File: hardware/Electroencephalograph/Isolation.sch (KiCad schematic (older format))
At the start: 5 parts, among them U6 ADUM2401BRWZ

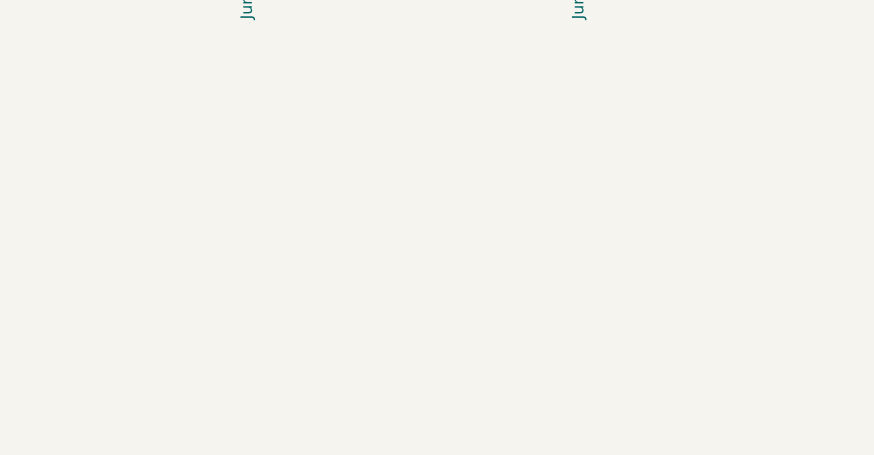
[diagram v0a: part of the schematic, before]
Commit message: power circuit supply added
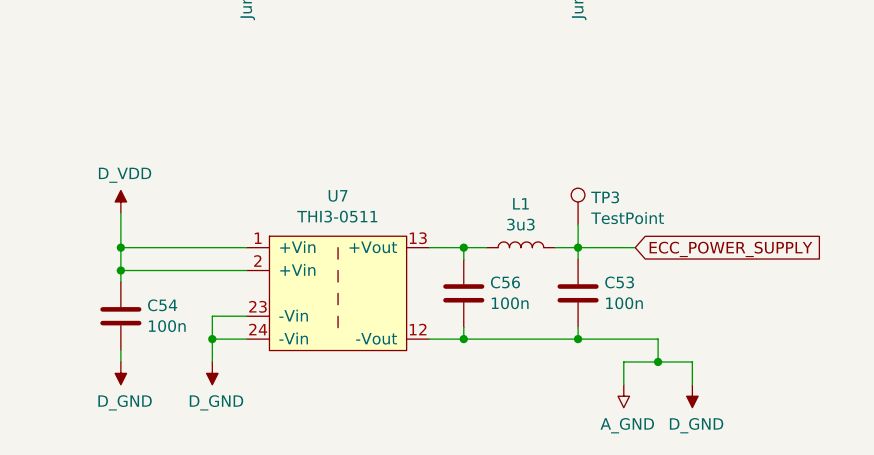
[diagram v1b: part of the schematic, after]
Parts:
- added C53, C54, C56: 100n, Capacitor_SMD:C_0402_1005Metric, symbol Device:C
- added L1: 3u3, Inductor_SMD:L_1206_3216Metric, symbol Device:L
- added TP3: TestPoint, TestPoint:TestPoint_Pad_1.5x1.5mm, symbol Connector:TestPoint
- added U7: THI3-0511, Relay_THT:Relay_DPDT_Omron_G6K-2P-Y, symbol Electroencephalograph:THI3-0511
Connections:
- net GNDA: now also C53.2, C54.2, C56.2, U7.12 (-Vout), U7.23 (-Vin), U7.24 (-Vin)
- net VDDA: now also C54.1, U7.1 (+Vin), U7.2 (+Vin)
- new net: C56.1, L1.1, U7.13 (+Vout)
- new net ECC_POWER_SUPPLY: C53.1, L1.2, TP3.1
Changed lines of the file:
@@
 $Descr A4 11693 8268
 encoding utf-8
-Sheet 5 5
+Sheet 5 6
 Title ""
 Date ""
@@
 	1    0    0    -1
 $EndComp
+$Comp
+L Electroencephalograph:THI3-0511 U7
+U 1 1 5E036623
+P 3200 4600
+F 0 "U7" H 3200 4625 50  0000 C CNN
+F 1 "THI3-0511" H 3200 4534 50  0000 C CNN
+F 2 "Relay_THT:Relay_DPDT_Omron_G6K-2P-Y" H 3200 4600 50  0001 C CNN
+F 3 "" H 3200 4600 50  0001 C CNN
+	1    3200 4600
+	1    0    0    -1
+$EndComp
+$Comp
+L Device:C C?
+U 1 1 5E036F39
+P 4250 5000
+AR Path="/5DF4CFF8/5E036F39" Ref="C?"  Part="1"
+AR Path="/5DF61103/5E036F39" Ref="C?"  Part="1"
+AR Path="/5DFE0AD6/5E036F39" Ref="C53"  Part="1"
+F 0 "C53" H 4365 5046 50  0000 L CNN
+F 1 "100n" H 4365 4955 50  0000 L CNN
+F 2 "Capacitor_SMD:C_0402_1005Metric" H 4288 4850 50  0001 C CNN
+F 3 "~" H 4250 5000 50  0001 C CNN
+	1    4250 5000
+	1    0    0    -1
+$EndComp
+$Comp
+L Device:C C?
+U 1 1 5E037D7B
+P 2250 5100
+AR Path="/5DF4CFF8/5E037D7B" Ref="C?"  Part="1"
+AR Path="/5DF61103/5E037D7B" Ref="C?"  Part="1"
+AR Path="/5DFE0AD6/5E037D7B" Ref="C54"  Part="1"
+F 0 "C54" H 2365 5146 50  0000 L CNN
+F 1 "100n" H 2365 5055 50  0000 L CNN
+F 2 "Capacitor_SMD:C_0402_1005Metric" H 2288 4950 50  0001 C CNN
+F 3 "~" H 2250 5100 50  0001 C CNN
+	1    2250 5100
+	1    0    0    -1
+$EndComp
+Wire Wire Line
+	2800 4800 2250 4800
+Wire Wire Line
+	2250 4800 2250 4900
+Wire Wire Line
+	2800 4900 2250 4900
+Connection ~ 2250 4900
+Wire Wire Line
+	2250 4900 2250 4950
+$Comp
+L Electroencephalograph:A_GND #PWR100
+U 1 1 5E03B175
+P 4450 5400
+F 0 "#PWR100" H 4450 5425 50  0001 C CNN
+F 1 "A_GND" H 4467 5227 50  0000 C CNN
+F 2 "" H 4450 5425 50  0001 C CNN
+F 3 "" H 4450 5425 50  0001 C CNN
+	1    4450 5400
+	1    0    0    -1
+$EndComp
+$Comp
+L Electroencephalograph:D_GND #PWR101
+U 1 1 5E03B5A4
+P 4750 5400
+F 0 "#PWR101" H 4750 5425 50  0001 C CNN
+F 1 "D_GND" H 4767 5227 50  0000 C CNN
+F 2 "" H 4750 5425 50  0001 C CNN
+F 3 "" H 4750 5425 50  0001 C CNN
+	1    4750 5400
+	1    0    0    -1
+$EndComp
+$Comp
+L Electroencephalograph:D_GND #PWR?
+U 1 1 5E03BC05
+P 2250 5300
+AR Path="/5DF61103/5E03BC05" Ref="#PWR?"  Part="1"
+AR Path="/5DFE0AD6/5E03BC05" Ref="#PWR98"  Part="1"
+F 0 "#PWR98" H 2250 5325 50  0001 C CNN
+F 1 "D_GND" H 2267 5127 50  0000 C CNN
+F 2 "" H 2250 5325 50  0001 C CNN
+F 3 "" H 2250 5325 50  0001 C CNN
+	1    2250 5300
+	1    0    0    -1
+$EndComp
+$Comp
+L Electroencephalograph:D_VDD #PWR?
+U 1 1 5E03C33A
+P 2250 4650
+AR Path="/5DF61103/5E03C33A" Ref="#PWR?"  Part="1"
+AR Path="/5DFE0AD6/5E03C33A" Ref="#PWR97"  Part="1"
+F 0 "#PWR97" H 2250 4775 50  0001 C CNN
+F 1 "D_VDD" H 2267 4823 50  0000 C CNN
+F 2 "" H 2250 4775 50  0001 C CNN
+F 3 "" H 2250 4775 50  0001 C CNN
+	1    2250 4650
+	1    0    0    -1
+$EndComp
+$Comp
+L Electroencephalograph:D_GND #PWR?
+U 1 1 5E03EA83
+P 2650 5300
+AR Path="/5DF61103/5E03EA83" Ref="#PWR?"  Part="1"
+AR Path="/5DFE0AD6/5E03EA83" Ref="#PWR99"  Part="1"
+F 0 "#PWR99" H 2650 5325 50  0001 C CNN
+F 1 "D_GND" H 2667 5127 50  0000 C CNN
+F 2 "" H 2650 5325 50  0001 C CNN
+F 3 "" H 2650 5325 50  0001 C CNN
+	1    2650 5300
+	1    0    0    -1
+$EndComp
+Wire Wire Line
+	2800 5100 2650 5100
+Wire Wire Line
+	2650 5100 2650 5200
+Wire Wire Line
+	2250 5300 2250 5250
+Wire Wire Line
+	2250 4800 2250 4650
+Connection ~ 2250 4800
+Wire Wire Line
+	4450 5300 4450 5400
+Wire Wire Line
+	4450 5300 4600 5300
+Wire Wire Line
+	4750 5300 4750 5400
+Wire Wire Line
+	2800 5200 2650 5200
+Connection ~ 2650 5200
+Wire Wire Line
+	2650 5200 2650 5300
+Wire Wire Line
+	4250 4800 4250 4850
+Wire Wire Line
+	3600 5200 3750 5200
+Wire Wire Line
+	4250 5200 4250 5150
+Wire Wire Line
+	4250 5200 4600 5200
+Wire Wire Line
+	4600 5200 4600 5300
+Connection ~ 4250 5200
+Connection ~ 4600 5300
+Wire Wire Line
+	4600 5300 4750 5300
+$Comp
+L Device:L L1
+U 1 1 5E061AC1
+P 4000 4800
+F 0 "L1" V 4190 4800 50  0000 C CNN
+F 1 "3u3" V 4099 4800 50  0000 C CNN
+F 2 "Inductor_SMD:L_1206_3216Metric" H 4000 4800 50  0001 C CNN
+F 3 "~" H 4000 4800 50  0001 C CNN
+	1    4000 4800
+	0    -1   -1   0
+$EndComp
+$Comp
+L Device:C C?
+U 1 1 5E064809
+P 3750 5000
+AR Path="/5DF4CFF8/5E064809" Ref="C?"  Part="1"
+AR Path="/5DF61103/5E064809" Ref="C?"  Part="1"
+AR Path="/5DFE0AD6/5E064809" Ref="C56"  Part="1"
+F 0 "C56" H 3865 5046 50  0000 L CNN
+F 1 "100n" H 3865 4955 50  0000 L CNN
+F 2 "Capacitor_SMD:C_0402_1005Metric" H 3788 4850 50  0001 C CNN
+F 3 "~" H 3750 5000 50  0001 C CNN
+	1    3750 5000
+	1    0    0    -1
+$EndComp
+Wire Wire Line
+	3600 4800 3750 4800
+Wire Wire Line
+	3750 4850 3750 4800
+Connection ~ 3750 4800
+Wire Wire Line
+	3750 4800 3850 4800
+Wire Wire Line
+	4150 4800 4250 4800
+Wire Wire Line
+	3750 5150 3750 5200
+Connection ~ 3750 5200
+Wire Wire Line
+	3750 5200 4250 5200
+Wire Wire Line
+	4250 4800 4500 4800
+Connection ~ 4250 4800
+Text GLabel 4500 4800 2    50   Input ~ 0
+ECC_POWER_SUPPLY
+$Comp
+L Connector:TestPoint TP?
+U 1 1 5E1B3787
+P 4250 4700
+AR Path="/5DF61103/5E1B3787" Ref="TP?"  Part="1"
+AR Path="/5DFE0AD6/5E1B3787" Ref="TP3"  Part="1"
+F 0 "TP3" H 4308 4818 50  0000 L CNN
+F 1 "TestPoint" H 4308 4727 50  0000 L CNN
+F 2 "TestPoint:TestPoint_Pad_1.5x1.5mm" H 4450 4700 50  0001 C CNN
+F 3 "~" H 4450 4700 50  0001 C CNN
+	1    4250 4700
+	1    0    0    -1
+$EndComp
+Wire Wire Line
+	4250 4700 4250 4800
 $EndSCHEMATC

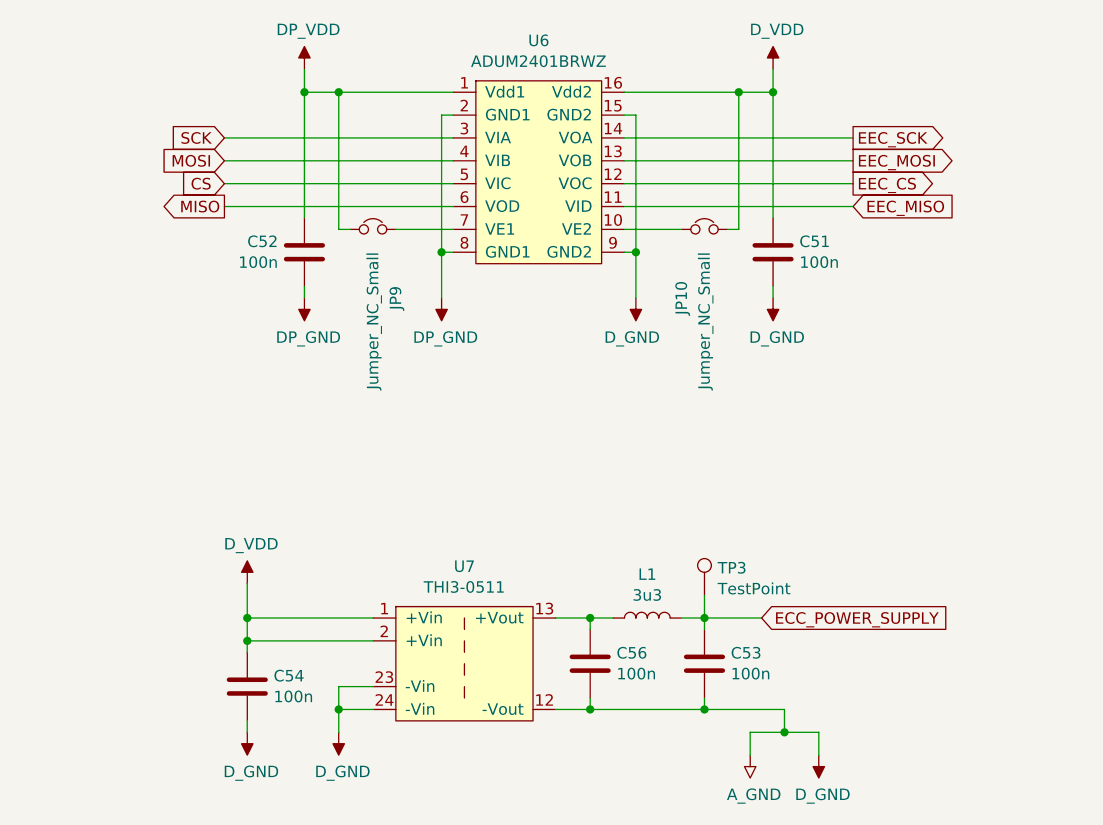
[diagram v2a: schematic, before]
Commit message: removed external clk and vref
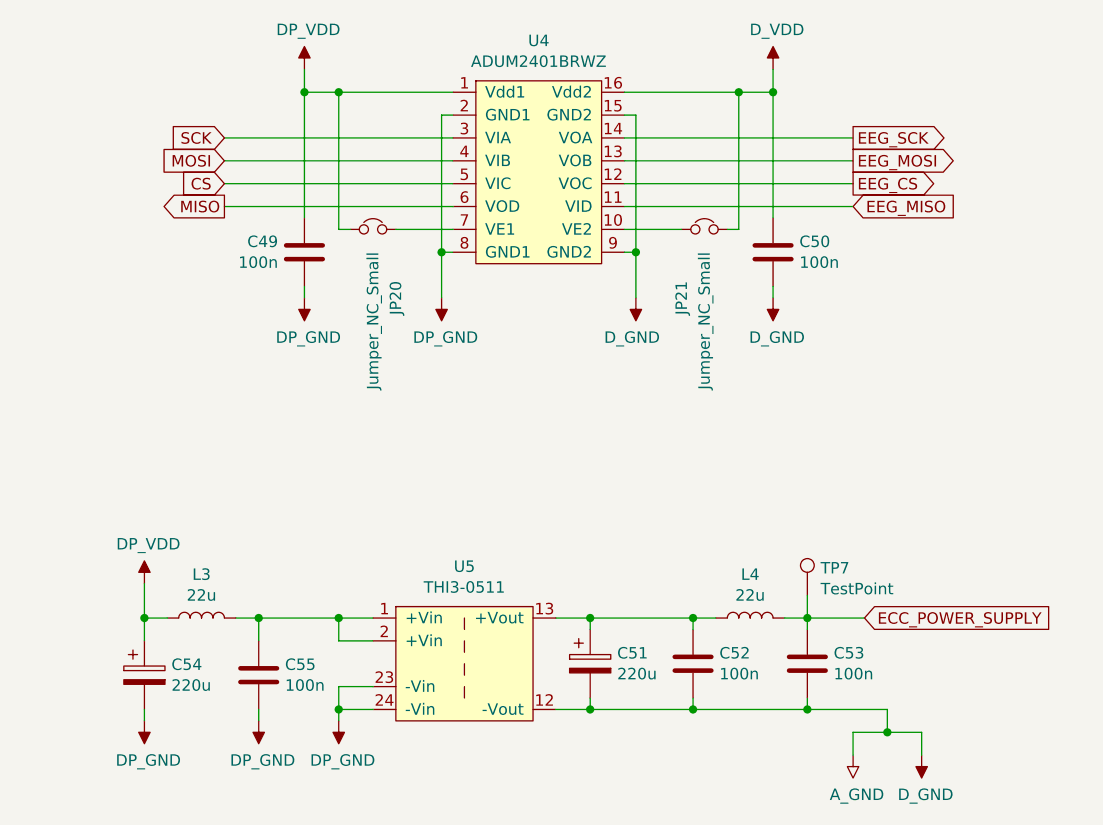
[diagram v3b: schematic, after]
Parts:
- added C51, C54: 220u, symbol Device:CP
- added L4: 22u, Inductor_SMD:L_7.3x7.3_H3.5, symbol Device:L
- L3: renamed from L1; value 3u3 -> 22u; footprint Inductor_SMD:L_1206_3216Metric -> Inductor_SMD:L_7.3x7.3_H3.5
- renumbered C52 to C49, C51 to C50, C56 to C52, C54 to C55, JP9 to JP20, JP10 to JP21, TP3 to TP7, U6 to U4, U7 to U5
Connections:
- net ECC_POWER_SUPPLY: now also L4.2; no longer L3.2
- net GNDA: now also C51.2, C54.2
- net VDDA: now also L3.1, C54.1; no longer C55.1, U5.1 (+Vin), U5.2 (+Vin)
- net at C52.1, U5.13 (+Vout): now also C51.1, L4.1; no longer L3.1
- net EEC_CS renamed EEG_CS
- net EEC_MISO renamed EEG_MISO
- net EEC_MOSI renamed EEG_MOSI
- net EEC_SCK renamed EEG_SCK
- new net: C55.1, L3.2, U5.1 (+Vin), U5.2 (+Vin)
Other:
- moved on the sheet: C52, C53, C55, L3, TP7

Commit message: bom simplification
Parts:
- C51, C54: footprint (none) -> Capacitor_SMD:CP_Elec_6.3x5.8
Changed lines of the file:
@@
 F 0 "C54" H 1918 5096 50  0000 L CNN
 F 1 "220u" H 1918 5005 50  0000 L CNN
-F 2 "" H 1838 4900 50  0001 C CNN
+F 2 "Capacitor_SMD:CP_Elec_6.3x5.8" H 1838 4900 50  0001 C CNN
 F 3 "~" H 1800 5050 50  0001 C CNN
 	1    1800 5050
@@
 F 0 "C51" H 3868 5046 50  0000 L CNN
 F 1 "220u" H 3868 4955 50  0000 L CNN
-F 2 "" H 3788 4850 50  0001 C CNN
+F 2 "Capacitor_SMD:CP_Elec_6.3x5.8" H 3788 4850 50  0001 C CNN
 F 3 "~" H 3750 5000 50  0001 C CNN
 	1    3750 5000

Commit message: draft of PCB routing
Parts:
- renumbered C54 to C49, C55 to C50, C49 to C51, C51 to C52, C52 to C53, C50 to C54, C53 to C55, JP20 to JP23, JP21 to JP24, TP7 to TP8, U5 to U4, U4 to U5
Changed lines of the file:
@@
 $EndDescr
 $Comp
-L Electroencephalograph:ADUM2401BRWZ U4
+L Electroencephalograph:ADUM2401BRWZ U5
 U 1 1 5E006D91
 P 3550 2350
-F 0 "U4" H 3525 2425 50  0000 C CNN
+F 0 "U5" H 3525 2425 50  0000 C CNN
 F 1 "ADUM2401BRWZ" H 3525 2334 50  0000 C CNN
 F 2 "Package_SO:SOIC-16W_7.5x10.3mm_P1.27mm" H 3550 2350 50  0001 C CNN
@@
 P 3950 3400
 AR Path="/5DF61103/5E009395" Ref="#PWR?"  Part="1"
-AR Path="/5DFE0AD6/5E009395" Ref="#PWR100"  Part="1"
-F 0 "#PWR100" H 3950 3425 50  0001 C CNN
+AR Path="/5DFE0AD6/5E009395" Ref="#PWR105"  Part="1"
+F 0 "#PWR105" H 3950 3425 50  0001 C CNN
 F 1 "D_GND" H 3967 3227 50  0000 C CNN
 F 2 "" H 3950 3425 50  0001 C CNN
@@
 P 4550 2400
 AR Path="/5DF61103/5E000D6D" Ref="#PWR?"  Part="1"
-AR Path="/5DFE0AD6/5E000D6D" Ref="#PWR97"  Part="1"
-F 0 "#PWR97" H 4550 2525 50  0001 C CNN
+AR Path="/5DFE0AD6/5E000D6D" Ref="#PWR106"  Part="1"
+F 0 "#PWR106" H 4550 2525 50  0001 C CNN
 F 1 "D_VDD" H 4567 2573 50  0000 C CNN
 F 2 "" H 4550 2525 50  0001 C CNN
@@
 P 4550 3400
 AR Path="/5DF61103/5E000D67" Ref="#PWR?"  Part="1"
-AR Path="/5DFE0AD6/5E000D67" Ref="#PWR101"  Part="1"
-F 0 "#PWR101" H 4550 3425 50  0001 C CNN
+AR Path="/5DFE0AD6/5E000D67" Ref="#PWR107"  Part="1"
+F 0 "#PWR107" H 4550 3425 50  0001 C CNN
 F 1 "D_GND" H 4567 3227 50  0000 C CNN
 F 2 "" H 4550 3425 50  0001 C CNN
@@
 AR Path="/5DF4CFF8/5E000D60" Ref="C?"  Part="1"
 AR Path="/5DF61103/5E000D60" Ref="C?"  Part="1"
-AR Path="/5DFE0AD6/5E000D60" Ref="C50"  Part="1"
-F 0 "C50" H 4665 3246 50  0000 L CNN
+AR Path="/5DFE0AD6/5E000D60" Ref="C54"  Part="1"
+F 0 "C54" H 4665 3246 50  0000 L CNN
 F 1 "100n" H 4665 3155 50  0000 L CNN
 F 2 "Capacitor_SMD:C_0402_1005Metric" H 4588 3050 50  0001 C CNN
@@
 $EndComp
 $Comp
-L Device:Jumper_NC_Small JP21
+L Device:Jumper_NC_Small JP24
 U 1 1 5E01EDC6
 P 4250 3100
-F 0 "JP21" V 4150 2800 50  0000 C CNN
+F 0 "JP24" V 4150 2800 50  0000 C CNN
 F 1 "Jumper_NC_Small" V 4250 2700 50  0000 C CNN
 F 2 "Jumper:SolderJumper-2_P1.3mm_Bridged_Pad1.0x1.5mm" H 4250 3100 50  0001 C CNN
@@
 AR Path="/5DF4CFF8/5E028BA8" Ref="C?"  Part="1"
 AR Path="/5DF61103/5E028BA8" Ref="C?"  Part="1"
-AR Path="/5DFE0AD6/5E028BA8" Ref="C49"  Part="1"
-F 0 "C49" H 2615 3246 50  0000 L CNN
+AR Path="/5DFE0AD6/5E028BA8" Ref="C51"  Part="1"
+F 0 "C51" H 2615 3246 50  0000 L CNN
 F 1 "100n" H 2615 3155 50  0000 L CNN
 F 2 "Capacitor_SMD:C_0402_1005Metric" H 2538 3050 50  0001 C CNN
@@
 $EndComp
 $Comp
-L Device:Jumper_NC_Small JP20
+L Device:Jumper_NC_Small JP23
 U 1 1 5E028BAE
 P 2800 3100
-F 0 "JP20" V 2700 2800 50  0000 C CNN
+F 0 "JP23" V 2700 2800 50  0000 C CNN
 F 1 "Jumper_NC_Small" V 2800 2700 50  0000 C CNN
 F 2 "Jumper:SolderJumper-2_P1.3mm_Bridged_Pad1.0x1.5mm" H 2800 3100 50  0001 C CNN
@@
 	2650 2500 2500 2500
 $Comp
-L Electroencephalograph:DP_GND #PWR99
+L Electroencephalograph:DP_GND #PWR104
 U 1 1 5E02E89B
 P 3100 3400
-F 0 "#PWR99" H 3100 3425 50  0001 C CNN
+F 0 "#PWR104" H 3100 3425 50  0001 C CNN
 F 1 "DP_GND" H 3117 3227 50  0000 C CNN
 F 2 "" H 3100 3425 50  0001 C CNN
@@
 $EndComp
 $Comp
-L Electroencephalograph:DP_GND #PWR98
+L Electroencephalograph:DP_GND #PWR102
 U 1 1 5E02EFAB
 P 2500 3400
-F 0 "#PWR98" H 2500 3425 50  0001 C CNN
+F 0 "#PWR102" H 2500 3425 50  0001 C CNN
 F 1 "DP_GND" H 2517 3227 50  0000 C CNN
 F 2 "" H 2500 3425 50  0001 C CNN
@@
 $EndComp
 $Comp
-L Electroencephalograph:DP_VDD #PWR96
+L Electroencephalograph:DP_VDD #PWR101
 U 1 1 5E02F433
 P 2500 2400
-F 0 "#PWR96" H 2500 2525 50  0001 C CNN
+F 0 "#PWR101" H 2500 2525 50  0001 C CNN
 F 1 "DP_VDD" H 2517 2573 50  0000 C CNN
 F 2 "" H 2500 2525 50  0001 C CNN
@@
 $EndComp
 $Comp
-L Electroencephalograph:THI3-0511 U5
+L Electroencephalograph:THI3-0511 U4
 U 1 1 5E036623
 P 3200 4600
-F 0 "U5" H 3200 4625 50  0000 C CNN
+F 0 "U4" H 3200 4625 50  0000 C CNN
 F 1 "THI3-0511" H 3200 4534 50  0000 C CNN
 F 2 "Relay_THT:Relay_DPDT_Omron_G6K-2P-Y" H 3200 4600 50  0001 C CNN
@@
 AR Path="/5DF4CFF8/5E036F39" Ref="C?"  Part="1"
 AR Path="/5DF61103/5E036F39" Ref="C?"  Part="1"
-AR Path="/5DFE0AD6/5E036F39" Ref="C53"  Part="1"
-F 0 "C53" H 4815 5046 50  0000 L CNN
+AR Path="/5DFE0AD6/5E036F39" Ref="C55"  Part="1"
+F 0 "C55" H 4815 5046 50  0000 L CNN
 F 1 "100n" H 4815 4955 50  0000 L CNN
 F 2 "Capacitor_SMD:C_0402_1005Metric" H 4738 4850 50  0001 C CNN
@@
 AR Path="/5DF4CFF8/5E037D7B" Ref="C?"  Part="1"
 AR Path="/5DF61103/5E037D7B" Ref="C?"  Part="1"
-AR Path="/5DFE0AD6/5E037D7B" Ref="C55"  Part="1"
-F 0 "C55" H 2415 5096 50  0000 L CNN
+AR Path="/5DFE0AD6/5E037D7B" Ref="C50"  Part="1"
+F 0 "C50" H 2415 5096 50  0000 L CNN
 F 1 "100n" H 2415 5005 50  0000 L CNN
 F 2 "Capacitor_SMD:C_0402_1005Metric" H 2338 4900 50  0001 C CNN
@@
 	2800 4900 2650 4900
 $Comp
-L Electroencephalograph:A_GND #PWR106
+L Electroencephalograph:A_GND #PWR108
 U 1 1 5E03B175
 P 4900 5400
-F 0 "#PWR106" H 4900 5425 50  0001 C CNN
+F 0 "#PWR108" H 4900 5425 50  0001 C CNN
 F 1 "A_GND" H 4917 5227 50  0000 C CNN
 F 2 "" H 4900 5425 50  0001 C CNN
@@
 $EndComp
 $Comp
-L Electroencephalograph:D_GND #PWR107
+L Electroencephalograph:D_GND #PWR109
 U 1 1 5E03B5A4
 P 5200 5400
-F 0 "#PWR107" H 5200 5425 50  0001 C CNN
+F 0 "#PWR109" H 5200 5425 50  0001 C CNN
 F 1 "D_GND" H 5217 5227 50  0000 C CNN
 F 2 "" H 5200 5425 50  0001 C CNN
@@
 AR Path="/5DF4CFF8/5E064809" Ref="C?"  Part="1"
 AR Path="/5DF61103/5E064809" Ref="C?"  Part="1"
-AR Path="/5DFE0AD6/5E064809" Ref="C52"  Part="1"
-F 0 "C52" H 4315 5046 50  0000 L CNN
+AR Path="/5DFE0AD6/5E064809" Ref="C53"  Part="1"
+F 0 "C53" H 4315 5046 50  0000 L CNN
 F 1 "100n" H 4315 4955 50  0000 L CNN
 F 2 "Capacitor_SMD:C_0402_1005Metric" H 4238 4850 50  0001 C CNN
@@
 P 4700 4700
 AR Path="/5DF61103/5E1B3787" Ref="TP?"  Part="1"
-AR Path="/5DFE0AD6/5E1B3787" Ref="TP7"  Part="1"
-F 0 "TP7" H 4758 4818 50  0000 L CNN
+AR Path="/5DFE0AD6/5E1B3787" Ref="TP8"  Part="1"
+F 0 "TP8" H 4758 4818 50  0000 L CNN
 F 1 "TestPoint" H 4758 4727 50  0000 L CNN
 F 2 "TestPoint:TestPoint_Pad_1.5x1.5mm" H 4900 4700 50  0001 C CNN
@@
 	4700 4700 4700 4800
 $Comp
-L Electroencephalograph:DP_VDD #PWR102
+L Electroencephalograph:DP_VDD #PWR98
 U 1 1 5E00C2CC
 P 1800 4650
-F 0 "#PWR102" H 1800 4775 50  0001 C CNN
+F 0 "#PWR98" H 1800 4775 50  0001 C CNN
 F 1 "DP_VDD" H 1817 4823 50  0000 C CNN
 F 2 "" H 1800 4775 50  0001 C CNN
@@
 $EndComp
 $Comp
-L Electroencephalograph:DP_GND #PWR105
+L Electroencephalograph:DP_GND #PWR103
 U 1 1 5E00C6AB
 P 2650 5250
-F 0 "#PWR105" H 2650 5275 50  0001 C CNN
+F 0 "#PWR103" H 2650 5275 50  0001 C CNN
 F 1 "DP_GND" H 2667 5077 50  0000 C CNN
 F 2 "" H 2650 5275 50  0001 C CNN
@@
 $EndComp
 $Comp
-L Electroencephalograph:DP_GND #PWR104
+L Electroencephalograph:DP_GND #PWR100
 U 1 1 5E00CF9A
 P 2300 5250
-F 0 "#PWR104" H 2300 5275 50  0001 C CNN
+F 0 "#PWR100" H 2300 5275 50  0001 C CNN
 F 1 "DP_GND" H 2317 5077 50  0000 C CNN
 F 2 "" H 2300 5275 50  0001 C CNN
@@
 $EndComp
 $Comp
-L Device:CP C54
+L Device:CP C49
 U 1 1 5E035319
 P 1800 5050
-F 0 "C54" H 1918 5096 50  0000 L CNN
+F 0 "C49" H 1918 5096 50  0000 L CNN
 F 1 "220u" H 1918 5005 50  0000 L CNN
 F 2 "Capacitor_SMD:CP_Elec_6.3x5.8" H 1838 4900 50  0001 C CNN
@@
 $EndComp
 $Comp
-L Electroencephalograph:DP_GND #PWR103
+L Electroencephalograph:DP_GND #PWR99
 U 1 1 5E03B877
 P 1800 5250
-F 0 "#PWR103" H 1800 5275 50  0001 C CNN
+F 0 "#PWR99" H 1800 5275 50  0001 C CNN
 F 1 "DP_GND" H 1817 5077 50  0000 C CNN
 F 2 "" H 1800 5275 50  0001 C CNN
@@
 	1800 4800 1800 4900
 $Comp
-L Device:CP C51
+L Device:CP C52
 U 1 1 5E0505FB
 P 3750 5000
-F 0 "C51" H 3868 5046 50  0000 L CNN
+F 0 "C52" H 3868 5046 50  0000 L CNN
 F 1 "220u" H 3868 4955 50  0000 L CNN
 F 2 "Capacitor_SMD:CP_Elec_6.3x5.8" H 3788 4850 50  0001 C CNN

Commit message: added inductor 3d model
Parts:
- L3, L4: footprint Inductor_SMD:L_7.3x7.3_H3.5 -> Electroencephalograph:L_7.3x7.3_H3.5
- U4: footprint Relay_THT:Relay_DPDT_Omron_G6K-2P-Y -> Electroencephalograph:THI3-0511
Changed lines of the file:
@@
 F 0 "U4" H 3200 4625 50  0000 C CNN
 F 1 "THI3-0511" H 3200 4534 50  0000 C CNN
-F 2 "Relay_THT:Relay_DPDT_Omron_G6K-2P-Y" H 3200 4600 50  0001 C CNN
-F 3 "" H 3200 4600 50  0001 C CNN
+F 2 "Electroencephalograph:THI3-0511" H 3200 4600 50  0001 C CNN
+F 3 "https://www.tme.eu/Document/dbc573554d903d2de79b1454bccf4b94/thi3-datasheet.pdf" H 3200 4600 50  0001 C CNN
 	1    3200 4600
 	1    0    0    -1
@@
 F 0 "L3" V 2240 4800 50  0000 C CNN
 F 1 "22u" V 2149 4800 50  0000 C CNN
-F 2 "Inductor_SMD:L_7.3x7.3_H3.5" H 2050 4800 50  0001 C CNN
+F 2 "Electroencephalograph:L_7.3x7.3_H3.5" H 2050 4800 50  0001 C CNN
 F 3 "~" H 2050 4800 50  0001 C CNN
 	1    2050 4800
@@
 F 0 "L4" V 4640 4800 50  0000 C CNN
 F 1 "22u" V 4549 4800 50  0000 C CNN
-F 2 "Inductor_SMD:L_7.3x7.3_H3.5" H 4450 4800 50  0001 C CNN
+F 2 "Electroencephalograph:L_7.3x7.3_H3.5" H 4450 4800 50  0001 C CNN
 F 3 "~" H 4450 4800 50  0001 C CNN
 	1    4450 4800
